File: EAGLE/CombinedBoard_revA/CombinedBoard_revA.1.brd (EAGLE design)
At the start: 53.6 x 76.2 mm, 80 parts, among them J1 U.FL-R-SMT-1_80_, J10 SM04B-SRSS-TB_LF__SN_, J11 HEADER_3PIN, J2 HEADER_5PIN, J2A HEADER_10PIN, J2B HEADER_10PIN, J3 DEBUG, J5 SOLAR, J6 S2B-PH-SM4-TB_LF__SN_, J7 SM04B-SRSS-TB_LF__SN_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

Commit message: Comstation JLC files
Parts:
- moved J10 3.59 mm to (34.8, 3.68)
- moved J7 3.50 mm to (42.4, 3.68)
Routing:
- net I2C_SCK: track 102.8 -> 101.1 mm
- net I2C_SDA: track 84.0 -> 82.3 mm
- net N$10: track 61.7 -> 61.2 mm

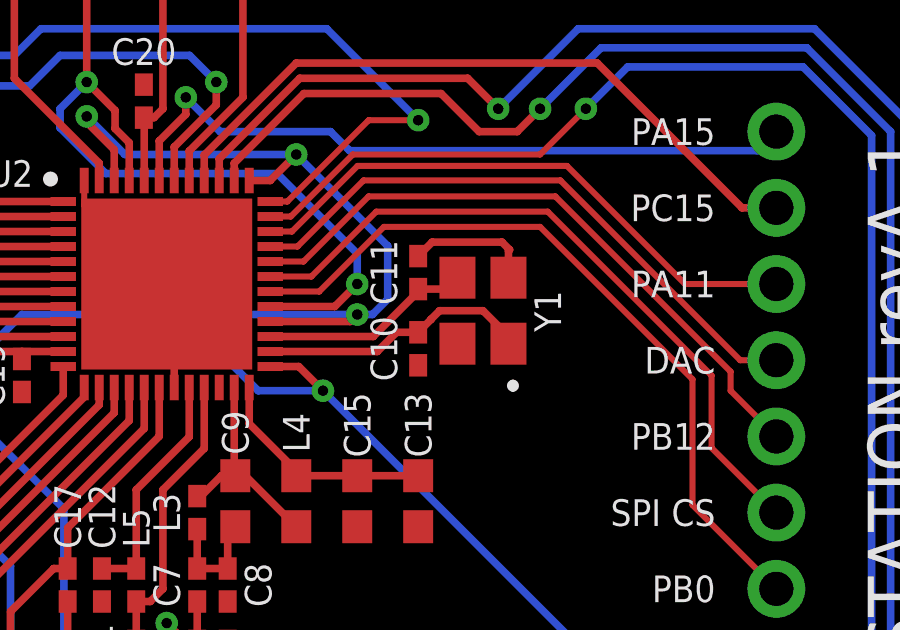
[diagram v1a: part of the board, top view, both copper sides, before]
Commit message: Comstation revA.1 error fix
fixed Y1 footprint
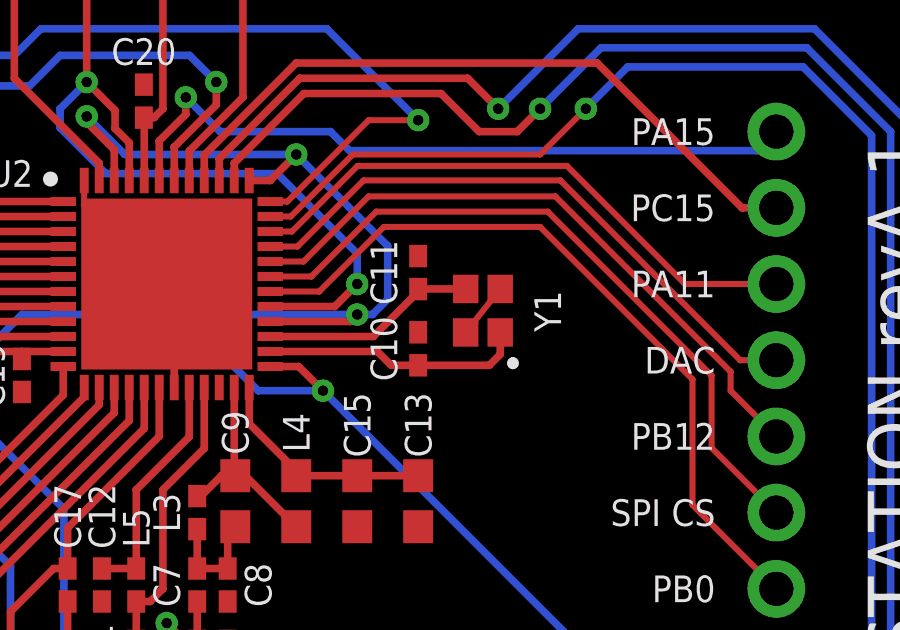
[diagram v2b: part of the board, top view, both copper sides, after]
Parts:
- Y1: device NSE LABS:SMD3225-4P -> NSE LABS:SMD2016-4P
- turned C10 to 90 degrees
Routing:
- net GND: track 30.8 -> 28.4 mm
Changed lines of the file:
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@@
 <drawing>
 <settings>
-<setting alwaysvectorfont="yes"/>
+<setting alwaysvectorfont="no"/>
 <setting verticaltext="up"/>
 </settings>
-<grid distance="0.005" unitdist="inch" unit="inch" style="lines" multiple="1" display="no" altdistance="5" altunitdist="mil" altunit="mil"/>
+<grid distance="0.001" unitdist="inch" unit="inch" style="lines" multiple="1" display="no" altdistance="5" altunitdist="mil" altunit="mil"/>
 <layers>
 <layer number="1" name="Top" color="4" fill="1" visible="yes" active="yes"/>
@@
 <attribute name="VALUE" x="22.225" y="19.177" size="1.27" layer="27" font="vector" rot="R270" align="center"/>
 </element>
-<element name="Y1" library="NSE LABS" package="SMD3225-4P" value="32MHz" x="37.338" y="28.321" smashed="yes" rot="R90">
+<element name="Y1" library="NSE LABS" package="SMD2016-4P" value="32MHz" x="37.338" y="28.321" smashed="yes" rot="R90">
 <attribute name="NAME" x="39.497" y="28.302" size="0.889" layer="25" font="vector" rot="R90" align="center"/>
 <attribute name="VALUE" x="39.878" y="27.921" size="1.27" layer="27" rot="R90" align="center"/>
 </element>
-<element name="C10" library="NSE LABS" package="0402" value="10pF" x="35.179" y="27.051" smashed="yes" rot="R270">
-<attribute name="NAME" x="34.036" y="27.051" size="0.889" layer="25" font="vector" rot="R90" align="center"/>
-<attribute name="VALUE" x="33.909" y="27.051" size="1.27" layer="27" font="vector" rot="R270" align="center"/>
+<element name="C10" library="NSE LABS" package="0402" value="10pF" x="35.179" y="27.051" smashed="yes" rot="R90">
+<attribute name="NAME" x="34.036" y="27.051" size="0.889" layer="25" font="vector" rot="R270" align="center"/>
+<attribute name="VALUE" x="36.449" y="27.051" size="1.27" layer="27" font="vector" rot="R90" align="center"/>
 </element>
 <element name="C11" library="NSE LABS" package="0402" value="10pF" x="35.179" y="29.591" smashed="yes" rot="R90">
@@
 <wire x1="24.047" y1="32.66" x2="24.047" y2="31.829" width="0.2032" layer="1"/>
 <wire x1="24.047" y1="31.829" x2="27.047" y2="28.829" width="0.2032" layer="1"/>
-<wire x1="35.179" y1="30.141" x2="35.645" y2="30.607" width="0.254" layer="1"/>
-<wire x1="37.973" y1="30.607" x2="38.227" y2="30.353" width="0.254" layer="1"/>
-<wire x1="38.227" y1="30.353" x2="38.188" y2="30.314" width="0.254" layer="1"/>
-<wire x1="38.188" y1="30.314" x2="38.188" y2="29.421" width="0.254" layer="1"/>
-<wire x1="35.645" y1="30.607" x2="37.973" y2="30.607" width="0.254" layer="1"/>
 <wire x1="27.122" y1="14.55" x2="27.122" y2="17.582" width="0.254" layer="1"/>
 <wire x1="27.122" y1="17.582" x2="26.797" y2="17.907" width="0.254" layer="1"/>
@@
 <wire x1="40.918" y1="5.844" x2="40.918" y2="6.961" width="0.254" layer="1"/>
 <wire x1="40.918" y1="6.961" x2="40.132" y2="7.747" width="0.254" layer="1"/>
+<wire x1="36.763" y1="27.596" x2="37.913" y2="29.046" width="0.2032" layer="1"/>
 </signal>
 <signal name="VDC">
@@
 <wire x1="35.179" y1="28.956" x2="35.179" y2="29.041" width="0.254" layer="1"/>
 <wire x1="33.683" y1="27.46" x2="35.179" y2="28.956" width="0.254" layer="1"/>
-<wire x1="35.179" y1="29.041" x2="36.108" y2="29.041" width="0.254" layer="1"/>
-<wire x1="36.108" y1="29.041" x2="36.488" y2="29.421" width="0.254" layer="1"/>
+<wire x1="36.763" y1="29.046" x2="35.184" y2="29.046" width="0.254" layer="1"/>
+<wire x1="35.184" y1="29.046" x2="35.179" y2="29.041" width="0.254" layer="1"/>
 </signal>
 <signal name="OSC_IN">
@@
 <contactref element="C10" pad="1"/>
 <wire x1="30.247" y1="26.96" x2="33.818" y2="26.96" width="0.254" layer="1"/>
-<wire x1="34.459" y1="27.601" x2="35.179" y2="27.601" width="0.254" layer="1"/>
-<wire x1="33.818" y1="26.96" x2="34.459" y2="27.601" width="0.254" layer="1"/>
-<wire x1="35.179" y1="27.601" x2="35.6086" y2="28.0306" width="0.254" layer="1"/>
-<wire x1="35.6086" y1="28.0306" x2="35.6086" y2="28.03673125" width="0.254" layer="1"/>
-<wire x1="35.6086" y1="28.03673125" x2="35.89286875" y2="28.321" width="0.254" layer="1"/>
-<wire x1="38.188" y1="27.471" x2="38.188" y2="27.221" width="0.254" layer="1"/>
-<wire x1="35.89286875" y1="28.321" x2="37.338" y2="28.321" width="0.254" layer="1"/>
-<wire x1="37.338" y1="28.321" x2="38.188" y2="27.471" width="0.254" layer="1"/>
+<wire x1="33.818" y1="26.96" x2="34.277" y2="26.501" width="0.254" layer="1"/>
+<wire x1="34.277" y1="26.501" x2="35.179" y2="26.501" width="0.254" layer="1"/>
+<wire x1="35.179" y1="26.501" x2="37.55" y2="26.501" width="0.254" layer="1"/>
+<wire x1="37.913" y1="26.864" x2="37.913" y2="27.596" width="0.254" layer="1"/>
+<wire x1="37.55" y1="26.501" x2="37.913" y2="26.864" width="0.254" layer="1"/>
 </signal>
 <signal name="N$5">
